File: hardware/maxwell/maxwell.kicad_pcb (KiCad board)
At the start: 2 copper layers, 122 x 59 mm, 96 parts, among them J1 Canbus 1, J10 SPI2_B, J11 BACKUP, J12 UART4, J13 UART5, J14 I2C1, J16 ESP_BM, J17 ESP_PROG, J19 Interconnect (Power), J2 SPI2_C, J20 Interconnect (uC), J3 Neopixel, J4 BOOT0, J5 SPI2_A, J6 Programmer, J7 Dynamo Input, J8 BOOT1, J9 Battery, Q1 BSS138, Q2 PSMN5R4-25YLD, Q3 DMG9926UDM, Q4 NTR1P02T1, Q5 NTR1P02T1, U1 MCP1501, U10 MIC39102, U11 AP9101C-SOT-25, U12 INA219AID, U13 PCF8593, U2 SN65HVD233, U3 TPS2113, U4 PCA9536D, U5 ESP-32S, U6 AD7991, U7 STM32F103RETx, U8 TLP188, U9 Buck Regulator, Y1 32.768k, Y2 8M

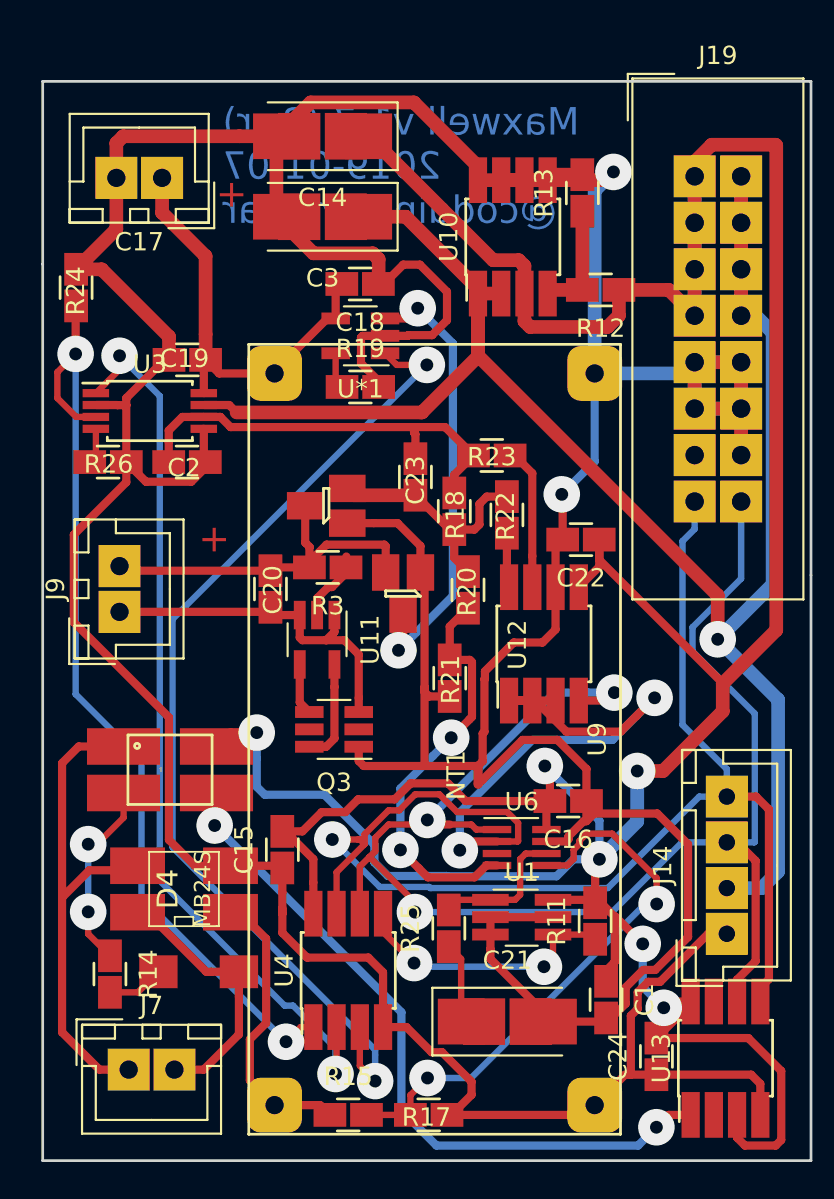
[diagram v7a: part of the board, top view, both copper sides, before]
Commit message: Revision 1.8a
* Collects regulated dynamo voltage via ADC channel 0.
* Swaps default power source from VBATT to VDYNAMO.  When charging, the
battery may have exactly the same voltage as the dynamo due to voltage
pulldown.  During such a scenario, we should use the dynamo.
* Adds previously missing pulldown resistor for open drain speed
input.
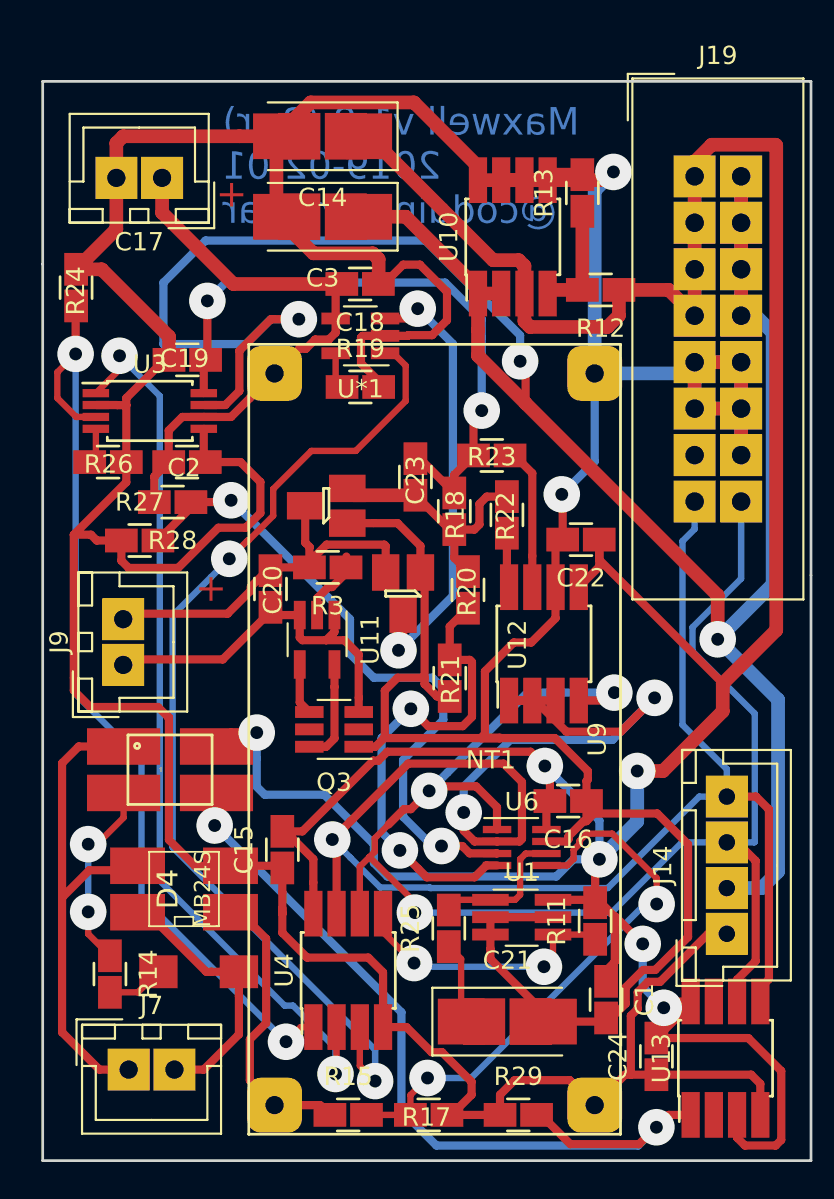
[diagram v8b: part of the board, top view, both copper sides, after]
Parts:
- added R27: ANY, coddingtonbear:0805_Milling, F.Cu at (62.3, 98.1)
- added R28: ANY, coddingtonbear:0805_Milling, F.Cu at (64.1, 96.0)
- added R29: 10k, coddingtonbear:0805_Milling, F.Cu at (83.0, 129.5)
- moved J9 2.91 mm to (61.4, 104.9)
- moved NT1 2.14 mm to (81.5, 108.9), turned to 180 degrees
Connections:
- net DISABLE_BATTERY_SRC renamed DISABLE_DYNAMO_SRC
- C19 pad 2: /Power/+Dynamo_Buck -> +BATT
- C2 pad 1: +BATT -> /Power/+Dynamo_Buck
- U3 pad 6: +BATT -> /Power/+Dynamo_Buck
- U3 pad 8: /Power/+Dynamo_Buck -> +BATT
- U6 pad 3: Net-(U6-Pad3) -> DYNAMO_REG_VOLTAGE
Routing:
- net DYNAMO_REG_VOLTAGE: track 0.00 -> 35.9 mm, vias 0 -> 2
- net VCC: track 299.2 -> 325.6 mm, vias 1 -> 3
- net GND: track 756.9 -> 771.4 mm
- net +BATT: track 23.8 -> 34.4 mm, vias 0 -> 2
- net /Power/+Dynamo_Buck: track 23.5 -> 31.7 mm
- net Net-(R29-Pad2): track 38.9 -> 46.5 mm
- net BATT_VOLTAGE: track 22.6 -> 26.5 mm
- net GNDA: track 45.0 -> 42.9 mm
- net I2C1_SDA: track 151.5 -> 153.2 mm
- net /Power/BATT-UNPROT: track 19.7 -> 20.7 mm
- net /Power/BATT+: track 20.4 -> 21.2 mm
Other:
- board text added: "Maxwell v1.8 (Pwr) 2019-02-01 @coddingtonbear"
- board text removed: "Maxwell v1.7 (Pwr) 2019-01-07 @coddingtonbear"
